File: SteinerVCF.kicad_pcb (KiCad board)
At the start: 2 copper layers, 39.6 x 100 mm, 78 parts, among them J1 AudioJack2_Ground_Switch, J2 AudioJack2_Ground_Switch, J3 AudioJack2_Ground_Switch, J4 AudioJack2_Ground_Switch, J5 Conn_02x05_Odd_Even, J6 AudioJack2_Ground_Switch, Q1 BC847, Q2 BC847, U1 TL072, U2 TL072, U3 TL072

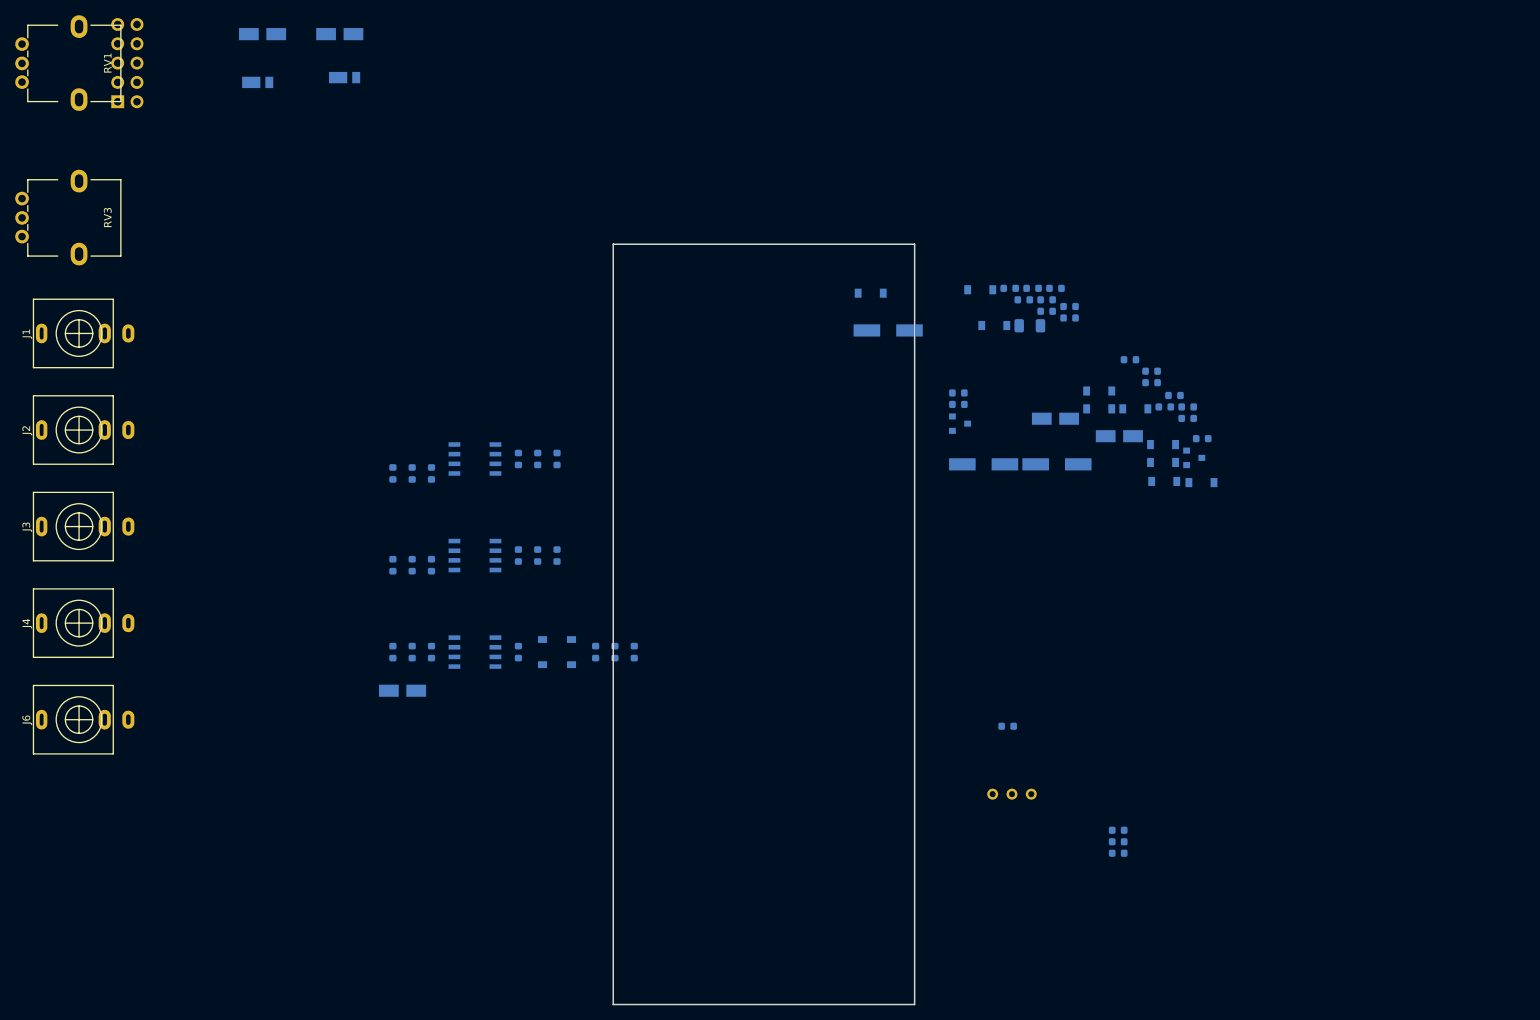
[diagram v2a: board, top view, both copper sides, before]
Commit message: Added footprints.
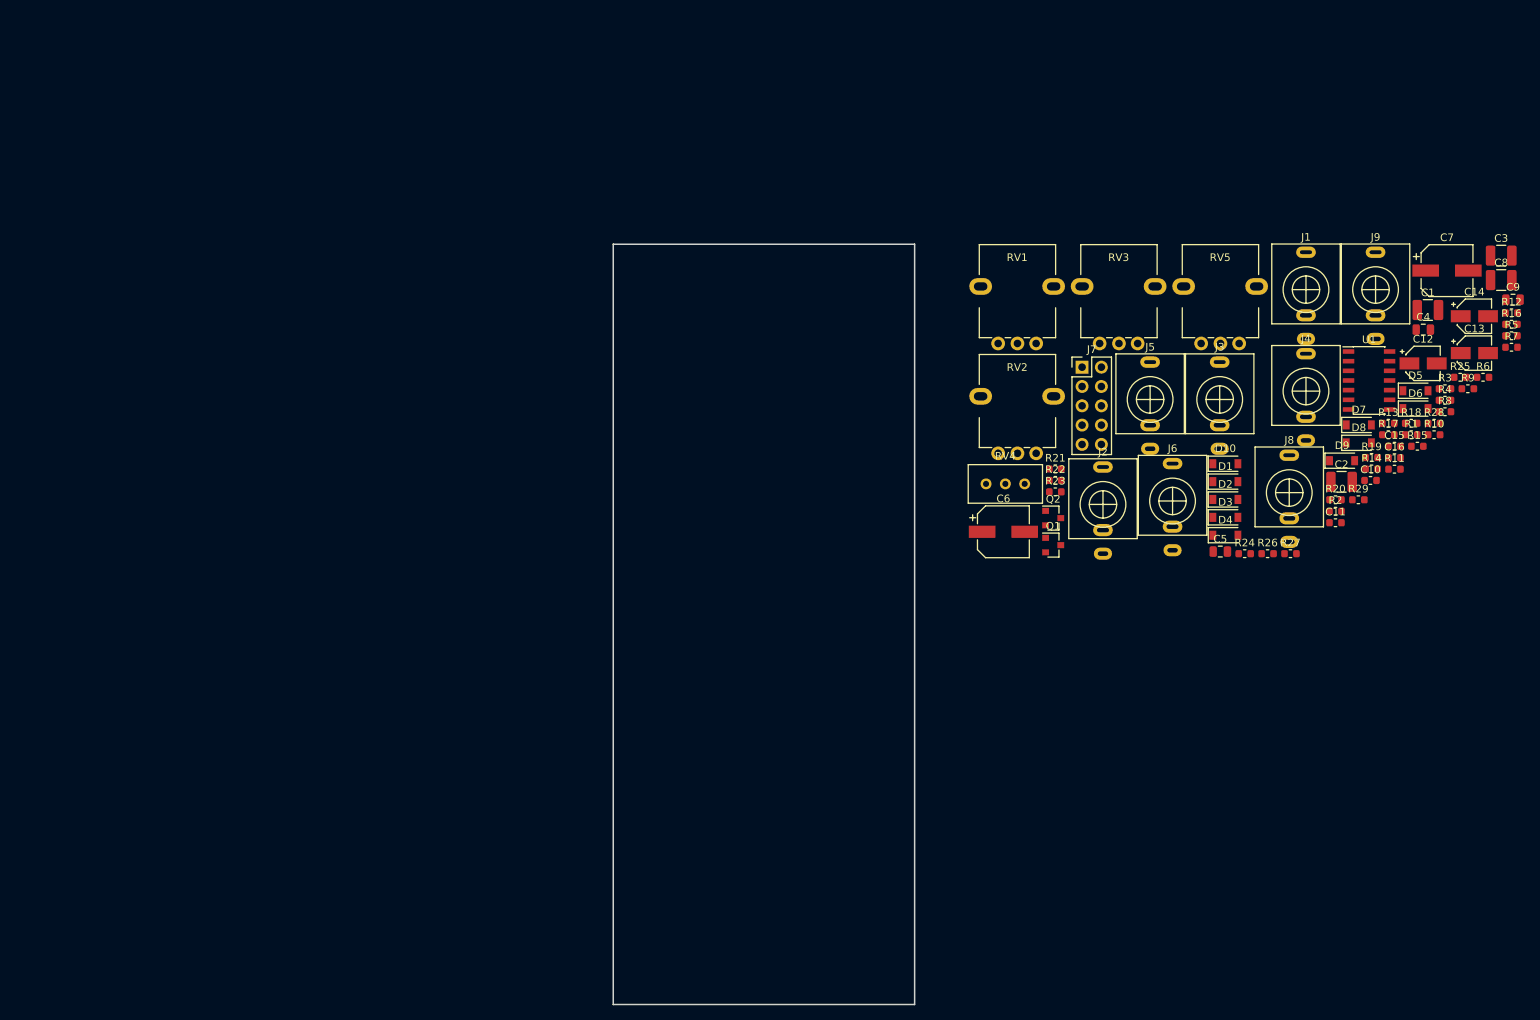
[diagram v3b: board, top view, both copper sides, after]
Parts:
- removed C17, C18: 100n, Capacitor_SMD:C_0603_1608Metric
- removed D11, D12, D13, D14: 1N4148W, Diode_SMD:D_SOD-123
- removed R30: 22k, Resistor_SMD:R_0603_1608Metric
- removed R31: 220k, Resistor_SMD:R_0603_1608Metric
- removed R32: 1k, Resistor_SMD:R_0603_1608Metric
- removed U2, U3: TL072, Package_SO:SOIC-8_3.9x4.9mm_P1.27mm
- added J7: Conn_02x05_Odd_Even, Connector_PinHeader_2.54mm:PinHeader_2x05_P2.54mm_Vertical, F.Cu at (190.3, 73.0)
- added J8: AudioJack2_Ground_Switch, Local:PJ398SM, F.Cu at (217.6, 89.5)
- added J9: AudioJack2_Ground_Switch, Local:PJ398SM, F.Cu at (228.9, 62.8)
- added RV4: 2k, Potentiometer_THT:Potentiometer_Bourns_3296W_Vertical, F.Cu at (182.8, 88.4)
- added RV5: 100k, Local:AlpsRK09K, F.Cu at (208.5, 62.4)
- C1, C2: value 100n -> 1u; footprint Capacitor_SMD:C_0603_1608Metric -> Capacitor_SMD:C_1210_3225Metric; moved to F.Cu
- C10: value 47u -> 100n; footprint Capacitor_SMD:CP_Elec_6.3x5.4 -> Capacitor_SMD:C_0603_1608Metric; moved to F.Cu
- C11: value 1.5n -> 100n; moved to F.Cu
- C12: value 680n -> 10u; footprint Capacitor_SMD:C_1206_3216Metric -> Capacitor_SMD:CP_Elec_4x5.8; moved to F.Cu
- C13: value 47u -> 10u; footprint Capacitor_SMD:CP_Elec_6.3x5.4 -> Capacitor_SMD:CP_Elec_4x5.8; moved to F.Cu
- C14, D1, D10, D2, D3, D4, D7, D8, D9, Q1, Q2, R1, R22: moved to F.Cu
- C15, C16: value 100n -> 22p; moved to F.Cu
- C3: value 10u -> 1u; footprint Capacitor_SMD:CP_Elec_4x5.8 -> Capacitor_SMD:C_1210_3225Metric; moved to F.Cu
- C4: value 10u -> 2n2; footprint Capacitor_SMD:CP_Elec_4x5.8 -> Capacitor_SMD:C_0805_2012Metric; moved to F.Cu
- C5: value 2.2u -> 2n2; footprint Capacitor_SMD:CP_Elec_4x5.4 -> Capacitor_SMD:C_0805_2012Metric; moved to F.Cu
- C6: value 2.2u -> 47u; footprint Capacitor_SMD:CP_Elec_4x5.4 -> Capacitor_SMD:CP_Elec_6.3x5.4; moved to F.Cu
- C7: value 1.5n -> 47u; footprint Capacitor_SMD:C_0603_1608Metric -> Capacitor_SMD:CP_Elec_6.3x5.4; moved to F.Cu
- C8: value 1.5n -> 1u; footprint Capacitor_SMD:C_0603_1608Metric -> Capacitor_SMD:C_1210_3225Metric; moved to F.Cu
- C9: value 47u -> 2n2; footprint Capacitor_SMD:CP_Elec_6.3x5.4 -> Capacitor_SMD:C_0805_2012Metric; moved to F.Cu
- D5, D6: value DFLR1400-7 -> 1N4148W; footprint Diode_SMD:D_PowerDI-123 -> Diode_SMD:D_SOD-123; moved to F.Cu
- J5: value Conn_02x05_Odd_Even -> AudioJack2_Ground_Switch; footprint Connector_PinHeader_2.54mm:PinHeader_2x05_P2.54mm_Vertical -> Local:PJ398SM; moved to F.Cu
- R10: value 47k -> 390; moved to F.Cu
- R11: value 47k -> 1k; moved to F.Cu
- R12: value 220k -> 1k; moved to F.Cu
- R13: value 180k -> 3K3; moved to F.Cu
- R14: value 180k -> 82; moved to F.Cu
- R15: value 1k8 -> 2k2; moved to F.Cu
- R16: value 3k9 -> 2200k; moved to F.Cu
- R17: value 82 -> 1k; moved to F.Cu
- R18: value 390 -> 22k; moved to F.Cu
- R19: value 1k -> 4K7; moved to F.Cu
- R2, R3, R4: value 100k -> 220k; moved to F.Cu
- R20: value 1k -> 100K; moved to F.Cu
- R21: value 1k8 -> 100K; moved to F.Cu
- R23: value 2200k -> 10k; moved to F.Cu
- R24: value 22k -> 6k8; moved to F.Cu
- R25: value 4k7 -> 33k; moved to F.Cu
- R26: value 1M -> 10k; moved to F.Cu
- R27: value 3k9 -> 10k; moved to F.Cu
- R28: value 220k -> 150k; moved to F.Cu
- R29: value 10k -> 1k; moved to F.Cu
- R5, R6, R7: value 100k -> 56k; moved to F.Cu
- R8: value 150k -> 2k2; moved to F.Cu
- R9: value 47k -> 470; moved to F.Cu
- RV2: value 1k -> 100k; footprint Potentiometer_THT:Potentiometer_Bourns_3296W_Vertical -> Local:AlpsRK09K; moved to F.Cu
- U1: value TL072 -> TL074; footprint Package_SO:SOIC-8_3.9x4.9mm_P1.27mm -> Package_SO:SOIC-14_3.9x8.7mm_P1.27mm; moved to F.Cu
- moved C3 165.5 mm to (245.5, 58.3)
- moved J4 164.2 mm to (219.8, 76.2), turned to 0 degrees
- moved J1 161.5 mm to (219.8, 62.8), turned to 0 degrees
- moved D5 157.6 mm to (234.2, 76.1)
- moved J3 151.0 mm to (208.4, 77.3), turned to 0 degrees
- moved C14 149.3 mm to (241.9, 66.3), turned to 0 degrees
- moved C4 147.7 mm to (235.2, 68.1)
- moved D6 147.4 mm to (234.2, 78.5)
- moved J6 146.7 mm to (202.2, 90.6), turned to 0 degrees
- moved J5 141.3 mm to (199.3, 77.3)
- moved R6 140.5 mm to (243.1, 74.3), turned to 0 degrees
- moved R10 138.0 mm to (236.6, 81.9), turned to 0 degrees
- moved R28 137.7 mm to (236.6, 80.4), turned to 0 degrees
- moved RV3 137.0 mm to (195.2, 62.4), turned to 0 degrees
- moved J2 135.0 mm to (193.1, 91.1), turned to 0 degrees
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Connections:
- C1 pad 1: +12V -> Net-(C1-Pad1)
- C1 pad 2: (no net) -> Net-(C1-Pad2)
- C10 pad 1: Net-(C10-Pad1) -> +12V
- C10 pad 2: (no net) -> GND
- C11 pad 1: Net-(C11-Pad1) -> GND
- C11 pad 2: Net-(C11-Pad2) -> -12V
- C13 pad 1: Net-(C13-Pad1) -> +12V
- C13 pad 2: Net-(C13-Pad2) -> GND
- C14 pad 1: Net-(C14-Pad1) -> GND
- C14 pad 2: Net-(C14-Pad2) -> -12V
- C15 pad 1: +12V -> Net-(C15-Pad1)
- C15 pad 2: (no net) -> Net-(C15-Pad2)
- C16 pad 1: (no net) -> Net-(C16-Pad1)
- C16 pad 2: -12V -> Net-(C16-Pad2)
- C2 pad 1: (no net) -> Net-(C2-Pad1)
- C2 pad 2: -12V -> Net-(C2-Pad2)
- C3 pad 1: +12V -> Net-(C3-Pad1)
- C3 pad 2: (no net) -> Net-(C3-Pad2)
- C4 pad 1: (no net) -> Net-(C4-Pad1)
- C4 pad 2: -12V -> Net-(C2-Pad1)
- C5 pad 1: Net-(C11-Pad2) -> Net-(C5-Pad1)
- C5 pad 2: Net-(C5-Pad2) -> Net-(C3-Pad1)
- C6 pad 1: Net-(C6-Pad1) -> GND
- C7 pad 2: Net-(C11-Pad2) -> GND
- C8 pad 1: Net-(C12-Pad2) -> Net-(C8-Pad1)
- C8 pad 2: Net-(C8-Pad2) -> Net-(C5-Pad1)
- C9 pad 1: (no net) -> Net-(C9-Pad1)
- C9 pad 2: Net-(C9-Pad2) -> Net-(C2-Pad1)
- D10 pad 1: Net-(C11-Pad1) -> Net-(C15-Pad1)
- D10 pad 2: Net-(D10-Pad2) -> Net-(C15-Pad2)
- D2 pad 2: Net-(D2-Pad2) -> Net-(C4-Pad1)
- D3 pad 1: Net-(D2-Pad2) -> Net-(C4-Pad1)
- D3 pad 2: Net-(C7-Pad1) -> Net-(D3-Pad2)
- D4 pad 1: Net-(C7-Pad1) -> Net-(D3-Pad2)
- D4 pad 2: Net-(D4-Pad2) -> Net-(C5-Pad1)
- D5 pad 1: +12V -> Net-(C5-Pad1)
- D6 pad 1: Net-(D6-Pad1) -> Net-(D5-Pad2)
- D6 pad 2: -12V -> Net-(C9-Pad1)
- D7 pad 1: Net-(D4-Pad2) -> Net-(C9-Pad1)
- D7 pad 2: Net-(C12-Pad2) -> Net-(D7-Pad2)
- D8 pad 1: Net-(C12-Pad2) -> Net-(D7-Pad2)
- D9 pad 1: Net-(D8-Pad2) -> Net-(C15-Pad2)
- D9 pad 2: Net-(C11-Pad1) -> Net-(C15-Pad1)
- J1 pad S: (no net) -> GND
- J1 pad T: Net-(J1-PadT) -> LoopIn
- J1 pad TN: Net-(J1-PadTN) -> LoopOut
- J2 pad S: (no net) -> GND
- J2 pad T: Net-(J2-PadT) -> /LP
- J3 pad S: (no net) -> GND
- J3 pad T: Net-(J3-PadT) -> /BP
- J4 pad S: (no net) -> GND
- J4 pad T: Net-(J4-PadT) -> /HP
- J6 pad S: (no net) -> GND
- J6 pad T: Net-(J6-PadT) -> /CV2
- Q2 pad 1: (no net) -> GND
- Q2 pad 3: Net-(D12-Pad2) -> Net-(D8-Pad2)
- R1 pad 2: Net-(J1-PadT) -> +12V
- R10 pad 1: Net-(C8-Pad2) -> +12V
- R10 pad 2: Net-(R10-Pad2) -> Net-(C7-Pad1)
- R11 pad 1: Net-(C5-Pad2) -> Net-(C1-Pad1)
- R11 pad 2: Net-(R11-Pad2) -> Net-(C7-Pad1)
- R12 pad 1: Net-(J4-PadT) -> Net-(C3-Pad1)
- R12 pad 2: Net-(Q1-Pad1) -> GND
- R13 pad 1: Net-(C6-Pad2) -> Net-(Q1-Pad2)
- R13 pad 2: (no net) -> Net-(C6-Pad2)
- R14 pad 1: Net-(C5-Pad2) -> Net-(C6-Pad2)
- R14 pad 2: (no net) -> -12V
- R15 pad 1: Net-(R15-Pad1) -> Net-(C1-Pad1)
- R15 pad 2: Net-(D1-Pad1) -> Net-(D8-Pad2)
- R16 pad 1: Net-(Q1-Pad2) -> Net-(C8-Pad1)
- R16 pad 2: Net-(C9-Pad2) -> GND
- R17 pad 1: Net-(C9-Pad2) -> Net-(R17-Pad1)
- R17 pad 2: -12V -> Net-(C2-Pad1)
- R18 pad 1: +12V -> Net-(R18-Pad1)
- R18 pad 2: Net-(C10-Pad1) -> GND
- R19 pad 1: Net-(C6-Pad1) -> Net-(C12-Pad1)
- R19 pad 2: Net-(C10-Pad1) -> Net-(R18-Pad1)
- R2 pad 2: Net-(J2-PadT) -> Net-(Q1-Pad1)
- R20 pad 1: Net-(C8-Pad2) -> /Resonance
- R20 pad 2: (no net) -> GND
- R21 pad 1: Net-(R21-Pad1) -> LoopIn
- R21 pad 2: Net-(D12-Pad2) -> Net-(R21-Pad2)
- R22 pad 1: Net-(R22-Pad1) -> LoopOut
- R22 pad 2: Net-(C11-Pad2) -> Net-(C12-Pad1)
- R23 pad 1: Net-(C12-Pad1) -> Net-(C15-Pad2)
- R23 pad 2: (no net) -> Net-(C12-Pad2)
- R24 pad 1: Net-(D13-Pad1) -> Net-(R24-Pad1)
- R24 pad 2: (no net) -> GND
- R25 pad 1: Net-(C13-Pad1) -> Net-(C15-Pad1)
- R25 pad 2: Net-(D13-Pad1) -> Net-(C15-Pad2)
- R26 pad 1: Net-(R26-Pad1) -> Net-(C16-Pad2)
- R26 pad 2: (no net) -> Net-(C15-Pad1)
- R27 pad 1: Net-(C13-Pad1) -> Net-(R27-Pad1)
- R27 pad 2: Net-(R27-Pad2) -> GND
- R28 pad 1: Net-(C14-Pad1) -> Net-(C16-Pad1)
- R28 pad 2: Net-(R26-Pad1) -> Net-(C16-Pad2)
- R29 pad 2: Net-(C13-Pad2) -> Net-(C16-Pad1)
- R3 pad 2: Net-(J3-PadT) -> Net-(Q1-Pad1)
- R4 pad 1: Net-(R4-Pad1) -> Net-(Q1-Pad1)
- R4 pad 2: +12V -> /CutOff
- R5 pad 1: Net-(R5-Pad1) -> Net-(C1-Pad2)
- R5 pad 2: Net-(R1-Pad1) -> /LP
- R6 pad 1: Net-(R10-Pad2) -> Net-(C2-Pad2)
- R6 pad 2: Net-(R2-Pad1) -> /BP
- R7 pad 1: Net-(R11-Pad2) -> Net-(C3-Pad2)
- R7 pad 2: Net-(R3-Pad1) -> /HP
- R8 pad 1: Net-(Q1-Pad1) -> Net-(C1-Pad1)
- R8 pad 2: Net-(R8-Pad2) -> Net-(D1-Pad1)
- R9 pad 1: Net-(C6-Pad2) -> Net-(Q1-Pad1)
- R9 pad 2: Net-(R5-Pad1) -> Net-(R9-Pad2)
- RV1 pad 1: Net-(R4-Pad1) -> Net-(R1-Pad1)
- RV1 pad 2: Net-(R8-Pad2) -> /CutOff
- RV1 pad 3: (no net) -> GND
- RV2 pad 1: Net-(R15-Pad1) -> /CV1
- RV2 pad 2: Net-(C6-Pad1) -> Net-(R2-Pad1)
- RV2 pad 3: Net-(R21-Pad1) -> GND
- RV3 pad 1: Net-(R27-Pad2) -> /CV2
- RV3 pad 2: Net-(C14-Pad2) -> Net-(R3-Pad1)
- RV3 pad 3: (no net) -> GND
- U1 pad 1: Net-(R10-Pad2) -> Net-(C12-Pad1)
- U1 pad 2: Net-(R2-Pad1) -> Net-(R18-Pad1)
- U1 pad 3: (no net) -> Net-(C8-Pad1)
- U1 pad 4: -12V -> +12V
- U1 pad 5: (no net) -> Net-(R21-Pad2)
- U1 pad 6: Net-(R1-Pad1) -> /Resonance
- U1 pad 7: Net-(R5-Pad1) -> Net-(R17-Pad1)
- U1 pad 8: +12V -> Net-(C15-Pad1)

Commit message: Initial component placement.
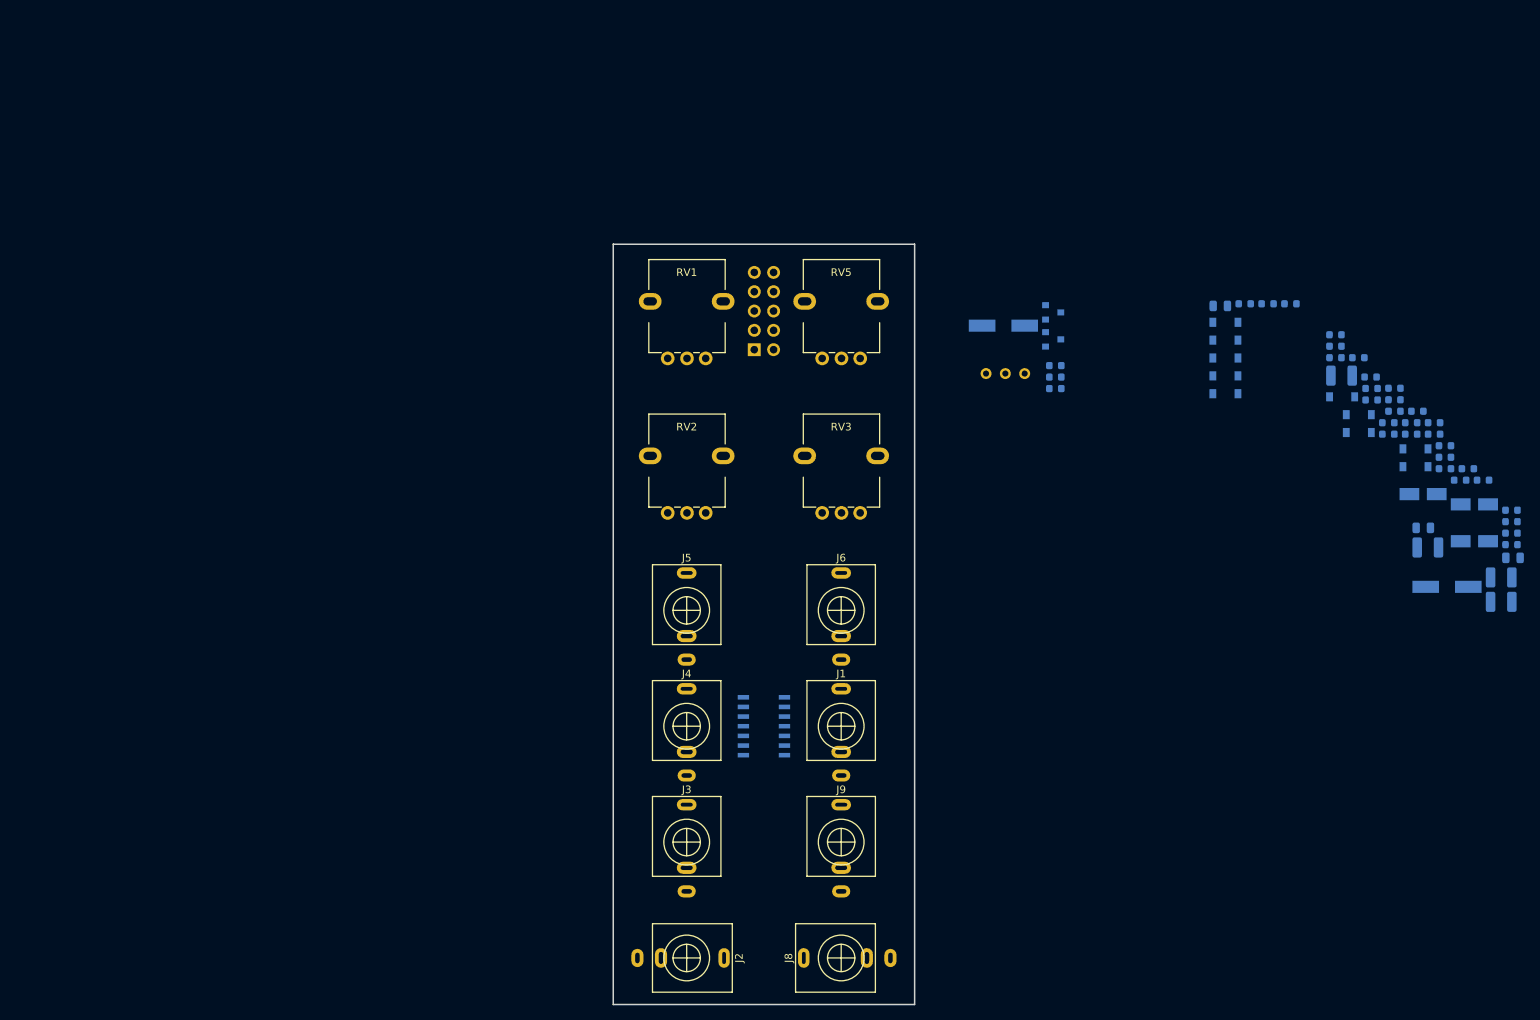
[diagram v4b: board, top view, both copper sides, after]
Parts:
- C1, C10, C11, C12, C13, C14, C15, C16, C2, C3, C4, C5, C6, C7, C8, C9, D1, D10, D2, D3, D4, D5, D6, D7, D8, D9, J7, Q1, Q2, R1, R10, R11, R12, R13, R14, R15, R16, R17, R18, R19, R2, R20, R21, R22, R23, R24, R25, R26, R27, R28, R29, R3, R4, R5, R6, R7, R8, R9, RV4, U1: moved to B.Cu
- moved J9 101.1 mm to (158.7, 135.5)
- moved J4 92.6 mm to (138.3, 120.2)
- moved U1 91.7 mm to (148.5, 120.2), turned to 180 degrees
- moved J3 91.1 mm to (138.3, 135.5)
- moved J8 85.0 mm to (158.7, 150.7), turned to 90 degrees
- moved J1 83.9 mm to (158.7, 120.2)
- moved J2 81.0 mm to (138.3, 150.7), turned to 270 degrees
- moved J5 67.0 mm to (138.3, 105.0)
- moved RV5 49.9 mm to (158.7, 64.4)
- moved J6 45.9 mm to (158.7, 105.0)
- moved C3 45.5 mm to (245.5, 103.9)
- moved RV2 44.2 mm to (138.3, 84.7)
- moved RV1 43.5 mm to (138.3, 64.4)
- moved J7 43.2 mm to (147.2, 70.7)
- moved RV3 42.8 mm to (158.7, 84.7)
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
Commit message: More placement.
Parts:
- moved R25 154.2 mm to (89.3, 120.2)
- moved C15 146.3 mm to (90.1, 116.4)
- moved R16 142.0 mm to (104.8, 98.7)
- moved D9 138.2 mm to (90.1, 108.8), turned to 180 degrees
- moved C12 136.3 mm to (101.5, 116.4)
- moved R18 130.2 mm to (104.0, 94.8)
- moved R19 129.9 mm to (99.8, 94.8)
- moved R24 124.6 mm to (101.5, 122.8)
- moved D10 124.5 mm to (90.1, 112.6)
- moved R5 123.9 mm to (138.3, 153.3)
- moved R6 117.4 mm to (135.8, 135.5), turned to 90 degrees
- moved C8 113.6 mm to (132.0, 105.0), turned to 90 degrees
- moved R7 111.8 mm to (138.3, 119.0), turned to 90 degrees
- moved C1 110.8 mm to (138.3, 149.4), turned to 270 degrees
- moved C9 108.9 mm to (138.3, 105.0), turned to 180 degrees
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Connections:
- C10 pad 2: GND -> (no net)
- C11 pad 1: GND -> (no net)
- C13 pad 2: GND -> (no net)
- C14 pad 1: GND -> (no net)
- C6 pad 1: GND -> (no net)
- C7 pad 2: GND -> (no net)
- J1 pad S: GND -> (no net)
- J2 pad S: GND -> (no net)
- J3 pad S: GND -> (no net)
- J4 pad S: GND -> (no net)
- J5 pad S: GND -> (no net)
- J6 pad S: GND -> (no net)
- J7 pad 3: GND -> (no net)
- J7 pad 4: GND -> (no net)
- J7 pad 5: GND -> (no net)
- J7 pad 6: GND -> (no net)
- J7 pad 7: GND -> (no net)
- J7 pad 8: GND -> (no net)
- J8 pad S: GND -> (no net)
- J9 pad S: GND -> (no net)
- Q2 pad 1: GND -> (no net)
- R12 pad 2: GND -> (no net)
- R16 pad 2: GND -> (no net)
- R18 pad 2: GND -> (no net)
- R20 pad 2: GND -> (no net)
- R24 pad 2: GND -> (no net)
- R27 pad 2: GND -> (no net)
- RV1 pad 3: GND -> (no net)
- RV2 pad 3: GND -> (no net)
- RV3 pad 3: GND -> (no net)
- RV4 pad 3: GND -> (no net)
- U1 pad 1: Net-(C12-Pad1) -> Net-(R17-Pad1)
- U1 pad 12: Net-(R27-Pad1) -> Net-(C8-Pad1)
- U1 pad 13: Net-(C16-Pad2) -> Net-(R18-Pad1)
- U1 pad 14: Net-(C16-Pad1) -> Net-(C12-Pad1)
- U1 pad 2: Net-(R18-Pad1) -> /Resonance
- U1 pad 3: Net-(C8-Pad1) -> Net-(R21-Pad2)
- U1 pad 5: Net-(R21-Pad2) -> Net-(R27-Pad1)
- U1 pad 6: /Resonance -> Net-(C16-Pad2)
- U1 pad 7: Net-(R17-Pad1) -> Net-(C16-Pad1)
